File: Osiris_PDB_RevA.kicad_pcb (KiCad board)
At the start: 4 copper layers, 127.5 x 65 mm, 69 parts, among them J1 MKDSP 25/2-15.00, J2 OSIRIS_I2C, J3 MKDSP 25/2-15.00, J4 XT60PW-F, Q1 ISC015N06NM5LF2, Q2 ISC015N06NM5LF2, Q3 BSC070N10NS5, U1 LTC4368HMS-1-PBF, U2 INA228AIDGSR, U3 LT3010EMS8E, U4 74AUP1G07GW, U5 LTC4359IMS8

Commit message: fixes 10.2.26
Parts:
- F1: value 4A MINI -> 7.5A MINI
- moved C9 5.00 mm to (175.5, 108.2), turned to 90 degrees
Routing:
- net /PDB_VOUT: track 92.4 -> 49.4 mm, vias 6 -> 0
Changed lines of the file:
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@@
 			)
 		)
-		(property "Selection_Status" "5 mOhm 1% 2 W four-terminal. Nominal breaker 10 A; normal-condition range 7.92-12.12 A. F1 remains 4 A; conductor/fuse coordination required."
+		(property "Selection_Status" "5 mOhm 1% 2 W four-terminal. Nominal breaker 10 A; normal-condition range 7.92-12.12 A. F1 is 7.5 A for a 5 A continuous avionics allowance; conductor/fuse coordination required."
 			(at 0 0 0)
 			(unlocked yes)
@@
 	(footprint "Capacitor_SMD:C_1206_3216Metric"
 		(layer "F.Cu")
-		(at 175.71 103.25 -90)
+		(at 175.5 108.25 90)
 		(descr "Capacitor SMD 1206 (3216 Metric), square (rectangular) end terminal, IPC-7351 nominal, (Body size source: IPC-SM-782 page 76, https://www.pcb-3d.com/wordpress/wp-content/uploads/ipc-sm-782a_amendment_1_and_2.pdf)")
 		(tags "capacitor")
@@
 		)
 		(property "Manufacturer" "TDK"
-			(at 0 0 270)
+			(at 0 0 90)
 			(unlocked yes)
 			(layer "F.Fab")
@@
 		)
 		(property "MPN" "C3216X7R1H106K160AC"
-			(at 0 0 270)
+			(at 0 0 90)
 			(unlocked yes)
 			(layer "F.Fab")
@@
 		)
 		(property "Selection_Status" "Output bulk capacitor; final total downstream capacitance and startup load must meet the proposed September 15 envelope. Inrush not qualified."
-			(at 0 0 270)
+			(at 0 0 90)
 			(unlocked yes)
 			(layer "F.Fab")
@@
 		(duplicate_pad_numbers_are_jumpers no)
 		(fp_line
-			(start -0.711252 0.91)
-			(end 0.711252 0.91)
+			(start -0.711252 -0.91)
+			(end 0.711252 -0.91)
 			(stroke
 				(width 0.12)
@@
 		)
 		(fp_line
-			(start -0.711252 -0.91)
-			(end 0.711252 -0.91)
+			(start -0.711252 0.91)
+			(end 0.711252 0.91)
 			(stroke
 				(width 0.12)
@@
 		)
 		(pad "1" smd roundrect
-			(at -1.475 0 270)
+			(at -1.475 0 90)
 			(size 1.15 1.8)
 			(layers "F.Cu" "F.Mask" "F.Paste")
@@
 		)
 		(pad "2" smd roundrect
-			(at 1.475 0 270)
+			(at 1.475 0 90)
 			(size 1.15 1.8)
 			(layers "F.Cu" "F.Mask" "F.Paste")
@@
 			)
 		)
-		(property "Value" "4A MINI"
+		(property "Value" "7.5A MINI"
 			(at 4.96 6.07 0)
 			(layer "F.Fab")
@@
 			)
 		)
-		(property "Description" "4 A, 32 VDC MINI blade fuse; backup protection for a fault the MOSFETs cannot interrupt"
+		(property "Description" "7.5 A, 32 VDC MINI blade fuse; backup protection for a fault the MOSFETs cannot interrupt"
 			(at 0 0 0)
 			(unlocked yes)
@@
 			)
 		)
-		(property "Selection_Status" "4 A 32 V MINI; load envelope 2.5 A maximum. Fuse, source and conductor coordination remains a release requirement."
+		(property "Selection_Status" "7.5 A 32 V MINI selected for 5 A continuous avionics allowance (67% of fuse rating). Electronic breaker remains nominally 10 A; fuse, source and conductor coordination remains a release requirement."
 			(at 0 0 0)
 			(unlocked yes)
@@
 			)
 		)
-		(property "MPN" "0297004.WXNV"
+		(property "MPN" "029707.5WXNV"
 			(at 0 0 0)
 			(unlocked yes)
@@
 	)
 	(segment
-		(start 175.135 112.925)
-		(end 179.335 112.925)
-		(width 3)
-		(layer "F.Cu")
-		(net "/PDB_VOUT")
-	)
-	(segment
-		(start 171.6375 92.15)
-		(end 176.2875 96.8)
-		(width 1)
-		(layer "F.Cu")
-		(net "/PDB_VOUT")
-	)
-	(segment
 		(start 167.239 106.536)
 		(end 167.239 97.3441)
@@
 	)
 	(segment
-		(start 179.46 96.8)
-		(end 179.46 97.75)
-		(width 1)
-		(layer "F.Cu")
-		(net "/PDB_VOUT")
-	)
-	(segment
-		(start 171.6375 109.4275)
-		(end 175.135 112.925)
-		(width 3)
-		(layer "F.Cu")
-		(net "/PDB_VOUT")
-	)
-	(segment
 		(start 171.6375 91.05)
 		(end 171.6375 92.3225)
@@
 	)
 	(segment
-		(start 179.46 97.75)
-		(end 175.71 101.5)
-		(width 1)
-		(layer "F.Cu")
-		(net "/PDB_VOUT")
-	)
-	(segment
 		(start 171.6375 91.05)
 		(end 171.6375 97.35)
@@
 	(segment
 		(start 171.6375 97.35)
-		(end 171.6375 109.4275)
-		(width 3)
-		(layer "F.Cu")
-		(net "/PDB_VOUT")
-	)
-	(segment
-		(start 171.6375 97.35)
 		(end 171.6375 97.4275)
 		(width 1)
@@
 	)
 	(segment
-		(start 171.6375 97.4275)
-		(end 175.71 101.5)
-		(width 1)
-		(layer "F.Cu")
-		(net "/PDB_VOUT")
-	)
-	(segment
 		(start 167.239 107)
 		(end 167.239 106.196)
@@
 	)
 	(segment
-		(start 176.2875 96.8)
-		(end 179.46 96.8)
-		(width 1)
-		(layer "F.Cu")
-		(net "/PDB_VOUT")
-	)
-	(segment
 		(start 171.6375 92.3225)
 		(end 168.46 95.5)
@@
 	)
 	(via
-		(at 176.46 98.75)
-		(size 0.6)
-		(drill 0.3)
-		(layers "F.Cu" "B.Cu")
-		(free yes)
-		(net "/PDB_VOUT")
-	)
-	(via
-		(at 176.71 94.75)
-		(size 0.6)
-		(drill 0.3)
-		(layers "F.Cu" "B.Cu")
-		(free yes)
-		(net "/PDB_VOUT")
-	)
-	(via
-		(at 168.46 98.5)
-		(size 0.6)
-		(drill 0.3)
-		(layers "F.Cu" "B.Cu")
-		(free yes)
-		(net "/PDB_VOUT")
-	)
-	(via
-		(at 175.71 96.5)
-		(size 0.6)
-		(drill 0.3)
-		(layers "F.Cu" "B.Cu")
-		(free yes)
-		(net "/PDB_VOUT")
-	)
-	(via
-		(at 168.46 95.5)
-		(size 0.6)
-		(drill 0.3)
-		(layers "F.Cu" "B.Cu")
-		(free yes)
-		(net "/PDB_VOUT")
-	)
-	(via
-		(at 175.46 98)
-		(size 0.6)
-		(drill 0.3)
-		(layers "F.Cu" "B.Cu")
-		(free yes)
-		(net "/PDB_VOUT")
-	)
-	(via
 		(at 131.9 82)
 		(size 1.2)
@@
 	)
 	(zone
+		(net "/PDB_VOUT")
+		(layer "F.Cu")
+		(hatch edge 0.5)
+		(priority 11)
+		(connect_pads yes
+			(clearance 0)
+		)
+		(min_thickness 0.1)
+		(fill yes
+			(thermal_gap 0.5)
+			(thermal_bridge_width 0.5)
+			(smoothing fillet)
+			(radius 0.1)
+			(island_removal_mode 0)
+		)
+		(polygon
+			(pts
+				(xy 170 100) (xy 170 116) (xy 183 116) (xy 183 109) (xy 174 109) (xy 174 100)
+			)
+		)
+	)
+	(zone
 		(net "/INPUT_DAMP")
 		(layer "F.Cu")
@@
 		(polygon
 			(pts
-				(xy 107.5 69) (xy 129.6 69) (xy 129.6 108) (xy 107.5 108)
+				(xy 107.5 69) (xy 129.6 69) (xy 129.6 103) (xy 122 103) (xy 122 108) (xy 118.55 108) (xy 107.5 108)
 			)
 		)
@@
 	(zone
 		(net "/PDB_VOUT")
-		(layers "F.Cu" "B.Cu")
+		(layer "F.Cu")
 		(hatch edge 0.5)
 		(priority 10)
-		(connect_pads
+		(connect_pads yes
 			(clearance 0)
 		)
-		(min_thickness 0.25)
+		(min_thickness 0.1)
 		(fill yes
 			(thermal_gap 0.5)
 			(thermal_bridge_width 0.5)
+			(smoothing fillet)
+			(radius 0.1)
 			(island_removal_mode 0)
 		)
 		(polygon
 			(pts
-				(xy 166.71 94.75) (xy 167.96 94.75) (xy 168.96 94.25) (xy 180.46 94.25) (xy 180 93.79) (xy 180 100.328571)
-				(xy 180.46 100) (xy 175.21 100) (xy 174.46 100.5) (xy 168.96 100.5) (xy 167.96 100) (xy 166.71 100)
+				(xy 168.25 94.75) (xy 168.25 94.25) (xy 174.5 94.25) (xy 174.5 100.5) (xy 168 100.5) (xy 168 103.25)
+				(xy 169.25 103.25) (xy 169.25 106.25) (xy 167.5 106.25) (xy 167.5 104) (xy 164.75 104) (xy 164.75 100.5)
+				(xy 166 100.5) (xy 166.0325 94.75)
 			)
 		)
@@
 	(zone
 		(net "/PDB_VOUT")
-		(layer "B.Cu")
+		(layers "F.Cu" "B.Cu")
 		(hatch edge 0.5)
-		(priority 12)
-		(connect_pads
-			(clearance 0.1)
+		(priority 11)
+		(connect_pads yes
+			(clearance 0)
 		)
-		(min_thickness 0.25)
+		(min_thickness 0.1)
 		(fill yes
 			(thermal_gap 0.5)
 			(thermal_bridge_width 0.5)
+			(smoothing fillet)
+			(radius 0.1)
 			(island_removal_mode 0)
 		)
 		(polygon
 			(pts
-				(xy 166.71 94.75) (xy 167.96 94.75) (xy 168.96 94.25) (xy 180.46 94.25) (xy 180 93.79) (xy 180 100.328571)
-				(xy 180.46 100) (xy 175.21 100) (xy 174.46 100.5) (xy 168.96 100.5) (xy 167.96 100) (xy 166.71 100)
+				(xy 170 94) (xy 170 116) (xy 183 116) (xy 183 109) (xy 174 109) (xy 174 94)
 			)
 		)

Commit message: Prepare PDB Rev A JLCPCB prototype manufacturing package
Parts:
- C11, C12, C13, C14, C15, C16: footprint Capacitor_THT:C_Rect_L7.2mm_W4.5mm_P5.00mm -> PDB_Footprints:C_Rect_L7.2mm_W4.5mm_P5.00mm_JLC
- J4: footprint Connector_AMASS:AMASS_XT60PW-F_1x02_P7.20mm_Horizontal -> PDB_Footprints:AMASS_XT60PW-F_1x02_P7.20mm_Horizontal

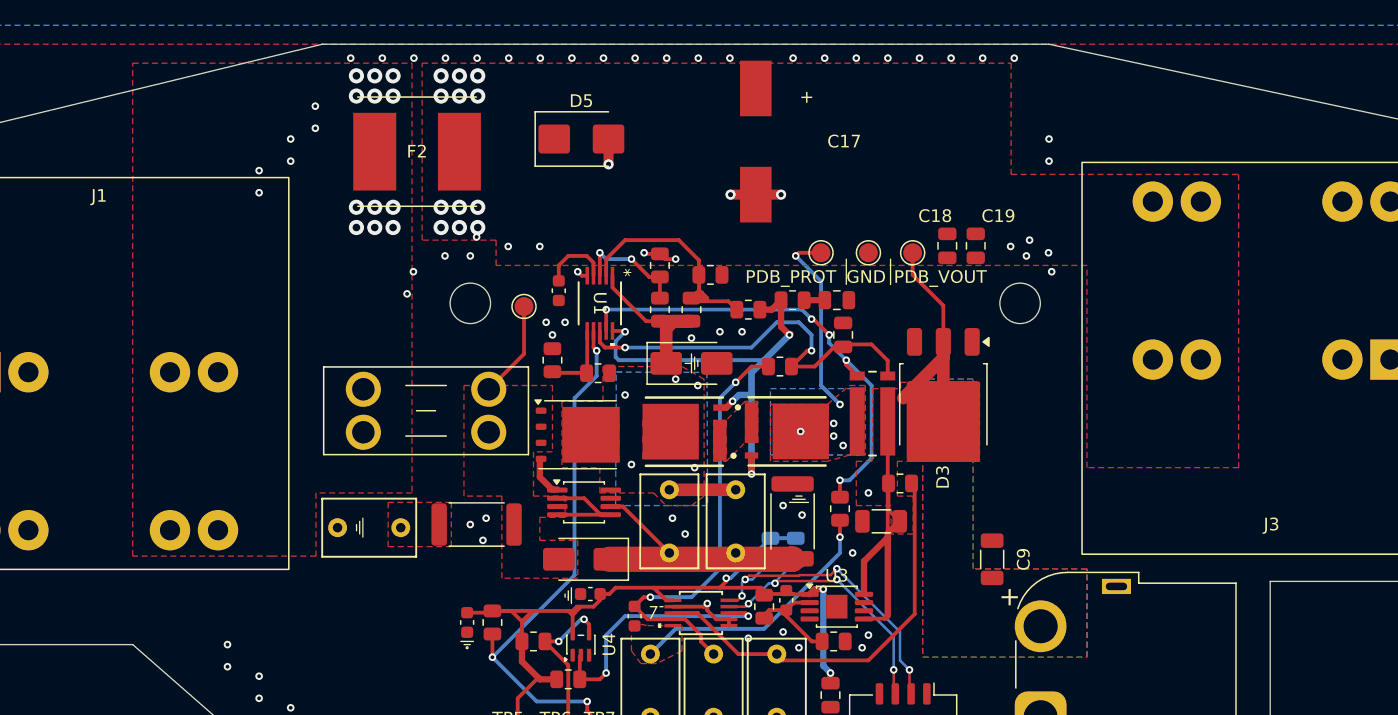
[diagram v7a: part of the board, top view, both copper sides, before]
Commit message: Add widened-copper 1 oz / 0.5 oz PDB test prototype
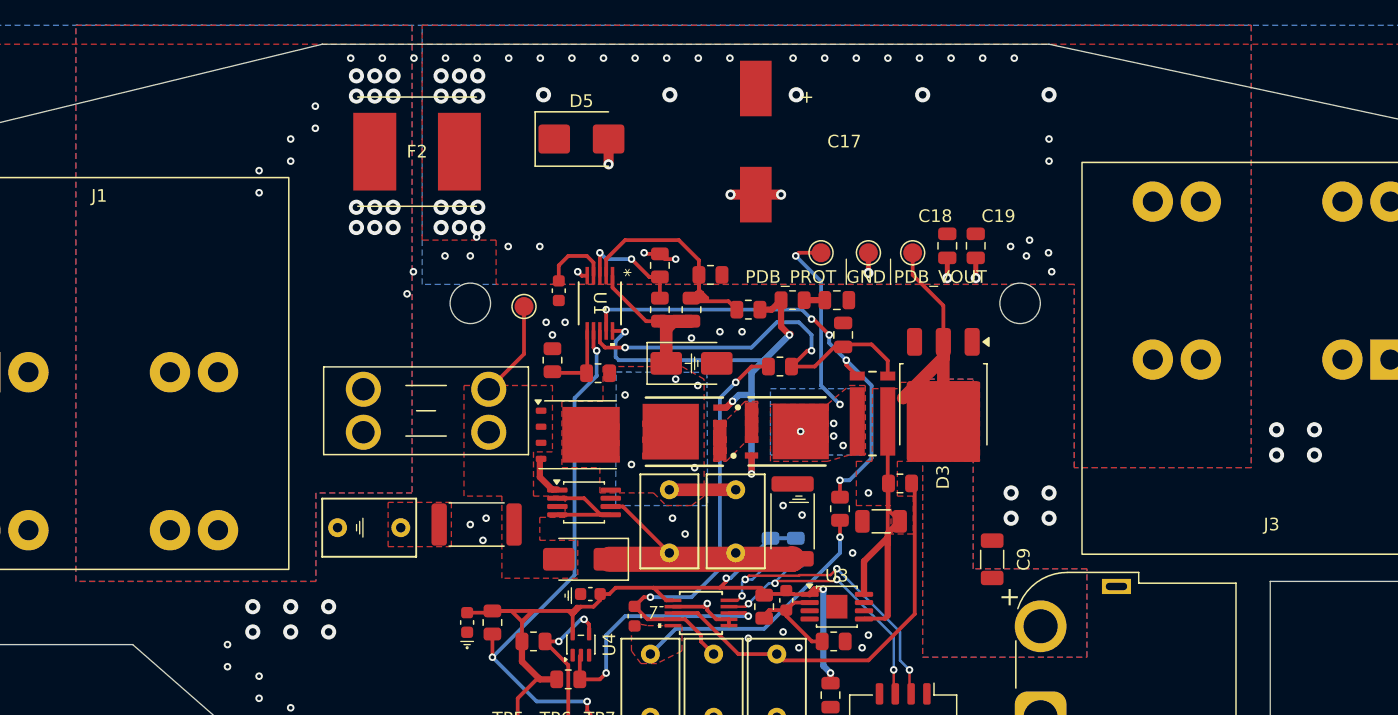
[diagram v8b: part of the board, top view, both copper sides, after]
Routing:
- net GND: track 15.5 -> 20.3 mm, vias 137 -> 157
- net /ESC_VBAT: vias 11 -> 13
- added copper zone on B.Cu, net /ESC_VBAT
- added copper zone on B.Cu, net /VBAT_RAW
- added copper zone on In2.Cu, net GND
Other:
- board text added: "LC TEST 1/0.5oz"
